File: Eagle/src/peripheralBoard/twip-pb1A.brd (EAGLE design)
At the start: 126.7 x 82.5 mm, 23 parts, among them J1 UJ2-BH-1-TH

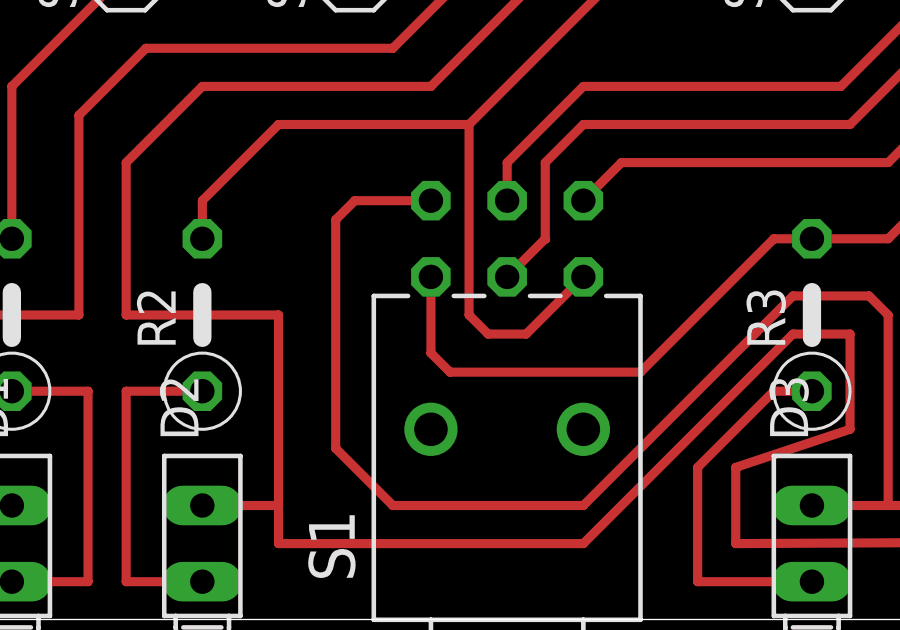
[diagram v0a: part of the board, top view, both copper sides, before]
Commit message: Update twip-pb1A.brd
bridge 5V grounds to get console working on battery power
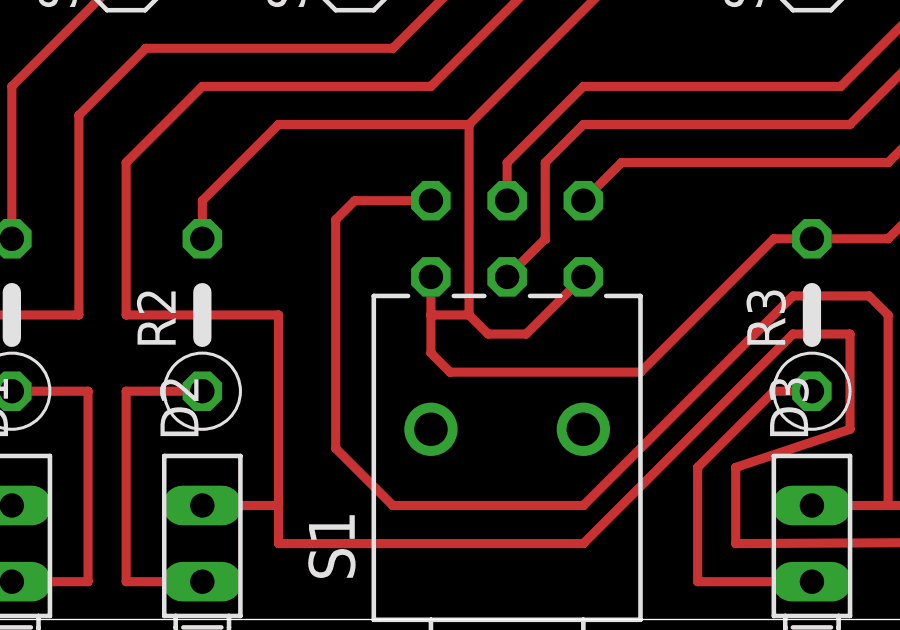
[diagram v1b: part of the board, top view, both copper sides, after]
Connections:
- removed net N$12: R2.2, S1.1, SV8.1
- net N$9: now also R2.2, S1.1, SV8.1
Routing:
- net N$9: track 34.7 -> 71.9 mm
- net N$12: track 36.0 -> 0.00 mm
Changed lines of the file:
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@@
 <wire x1="40.005" y1="59.055" x2="40.005" y2="67.31" width="0.3048" layer="1"/>
-</signal>
-<signal name="N$12">
-<contactref element="SV8" pad="1"/>
-<contactref element="R2" pad="2"/>
-<contactref element="S1" pad="1"/>
-<wire x1="43.18" y1="53.34" x2="49.53" y2="53.34" width="0.3048" layer="1"/>
-<wire x1="31.75" y1="48.26" x2="29.21" y2="45.72" width="0.3048" layer="1"/>
-<wire x1="29.21" y1="44.45" x2="29.21" y2="45.72" width="0.3048" layer="1"/>
-<wire x1="40.005" y1="41.275" x2="41.91" y2="43.18" width="0.3048" layer="1"/>
-<wire x1="38.735" y1="41.275" x2="38.1" y2="41.91" width="0.3048" layer="1"/>
-<wire x1="38.735" y1="41.275" x2="40.005" y2="41.275" width="0.3048" layer="1"/>
-<wire x1="31.75" y1="48.26" x2="38.1" y2="48.26" width="0.3048" layer="1"/>
-<wire x1="38.1" y1="48.26" x2="43.18" y2="53.34" width="0.3048" layer="1"/>
-<wire x1="38.1" y1="41.91" x2="38.1" y2="48.26" width="0.3048" layer="1"/>
 </signal>
 <signal name="N$14">
@@
 <contactref element="R3" pad="2"/>
 <contactref element="J1" pad="1"/>
-<wire x1="36.83" y1="43.18" x2="36.83" y2="40.64" width="0.3048" layer="1"/>
+<wire x1="36.83" y1="43.18" x2="36.83" y2="41.91" width="0.3048" layer="1"/>
+<wire x1="36.83" y1="41.91" x2="36.83" y2="40.64" width="0.3048" layer="1"/>
 <wire x1="43.815" y1="40.005" x2="48.26" y2="44.45" width="0.3048" layer="1"/>
 <wire x1="48.26" y1="44.45" x2="49.53" y2="44.45" width="0.3048" layer="1"/>
@@
 <wire x1="36.83" y1="40.64" x2="37.465" y2="40.005" width="0.3048" layer="1"/>
 <wire x1="37.465" y1="40.005" x2="43.815" y2="40.005" width="0.3048" layer="1"/>
+<contactref element="SV8" pad="1"/>
+<contactref element="R2" pad="2"/>
+<contactref element="S1" pad="1"/>
+<wire x1="43.18" y1="53.34" x2="49.53" y2="53.34" width="0.3048" layer="1"/>
+<wire x1="31.75" y1="48.26" x2="29.21" y2="45.72" width="0.3048" layer="1"/>
+<wire x1="29.21" y1="44.45" x2="29.21" y2="45.72" width="0.3048" layer="1"/>
+<wire x1="40.005" y1="41.275" x2="41.91" y2="43.18" width="0.3048" layer="1"/>
+<wire x1="38.735" y1="41.275" x2="38.1" y2="41.91" width="0.3048" layer="1"/>
+<wire x1="38.735" y1="41.275" x2="40.005" y2="41.275" width="0.3048" layer="1"/>
+<wire x1="31.75" y1="48.26" x2="38.1" y2="48.26" width="0.3048" layer="1"/>
+<wire x1="38.1" y1="48.26" x2="43.18" y2="53.34" width="0.3048" layer="1"/>
+<wire x1="38.1" y1="41.91" x2="38.1" y2="48.26" width="0.3048" layer="1"/>
+<wire x1="36.83" y1="41.91" x2="38.1" y2="41.91" width="0.3048" layer="1"/>
 </signal>
 <signal name="N$30">
